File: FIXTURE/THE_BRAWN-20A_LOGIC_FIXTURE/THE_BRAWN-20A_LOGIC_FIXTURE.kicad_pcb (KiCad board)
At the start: 2 copper layers, 100 x 100 mm, 59 parts, among them J1 Pins_2.54_1x3, J2 Pins_2.54_1x3, J5 Pins_2.54_1x2, M1 Mount_M3, M10 Mount_M3, M11 Mount_M3, M12 Mount_M3, M13 Mount_M3, M14 Mount_M3, M2 Mount_M3, M3 Mount_M3, M4 Mount_M3, M5 Mount_M3, M6 Mount_M3, M7 Mount_M3, M8 Mount_M3, M9 Mount_M3

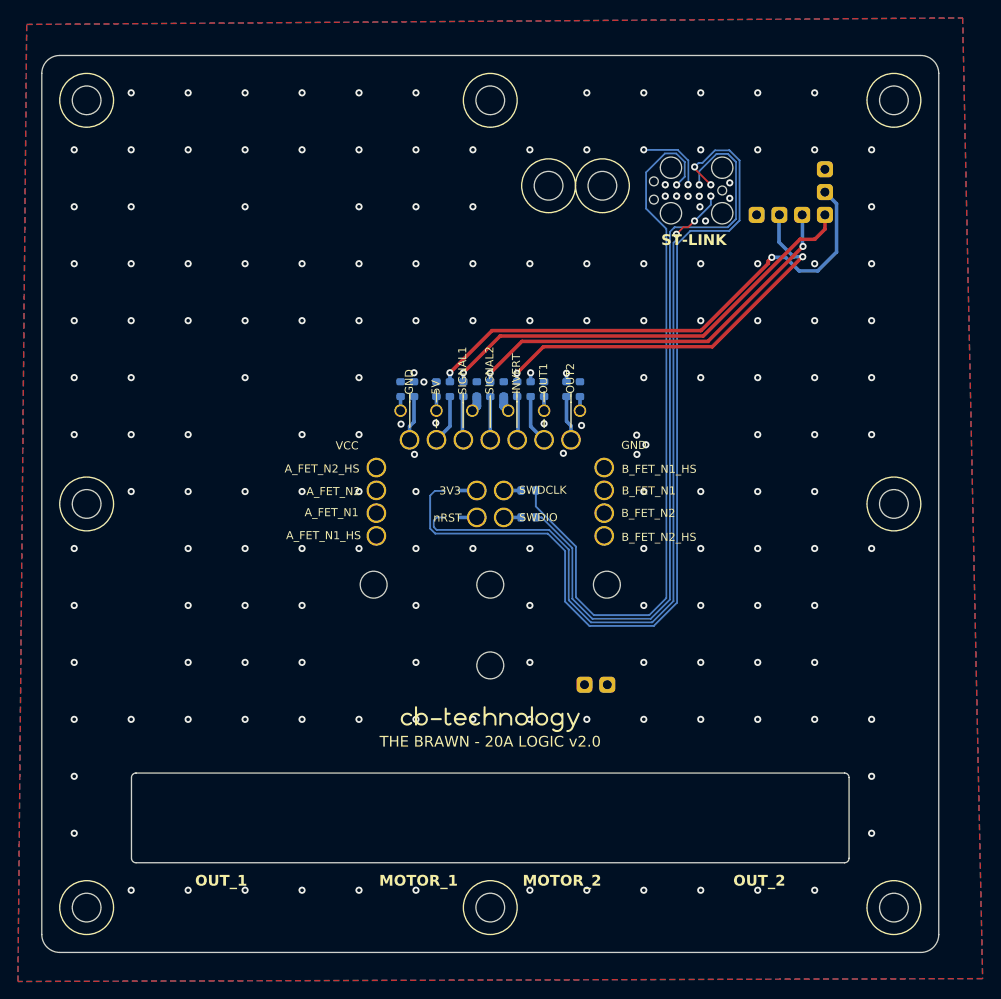
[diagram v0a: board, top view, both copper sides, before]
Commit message: Finish Tracking Logic Fixture PCB
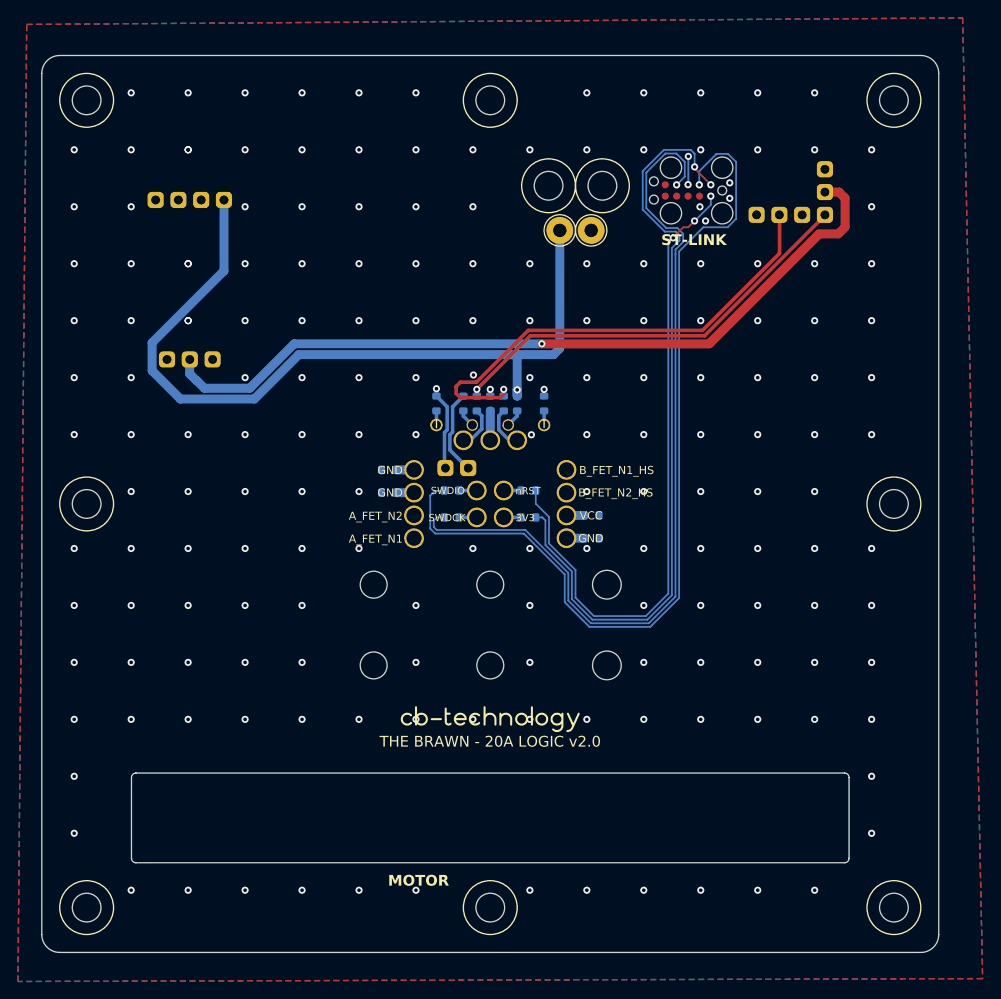
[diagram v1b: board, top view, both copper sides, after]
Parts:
- removed the R12 at (224.5, 127.2)
- removed the R13 at (228.5, 127.2)
- removed the TP14 at (210.0, 129.6)
- removed the TP15 at (214.0, 132.8)
- removed TP23, TP25, TP26, TP27: TestPoint, TestPoint:TestPoint_THTPad_D3.0mm_Drill1.5mm
- added J3: Pins_2.54_1x4, .J_Connector:Pins-2.54-1x4, B.Cu at (190.3, 106.1)
- added J4: Pins_2.54_1x3, .J_Connector:Pins-2.54-1x3, B.Cu at (189.0, 123.9)
- added M15: Mount_M3, .M_Mechanical:Mount_M3, F.Cu at (233.0, 149.0)
- added M16: Mount_M3, .M_Mechanical:Mount_M3, F.Cu at (233.0, 158.0)
- added R14: 0R, .R_Resistor:R_0603, B.Cu at (231.3, 141.3)
- added R15: 0R, .R_Resistor:R_0603, B.Cu at (231.3, 143.8)
- added TP16: TestPoint, TestPoint:TestPoint_THTPad_D3.0mm_Drill1.5mm, F.Cu at (227.8, 109.5)
- added TP17: TestPoint, TestPoint:TestPoint_THTPad_D3.0mm_Drill1.5mm, F.Cu at (231.2, 109.5)
- moved J5 28.7 mm to (215.0, 136.0)
- moved M14 27.5 mm to (207.0, 158.0)
- moved R6 20.2 mm to (215.7, 141.5), turned to 0 degrees
- moved R5 15.3 mm to (215.7, 138.5), turned to 0 degrees
- moved R2 12.7 mm to (208.7, 138.7), turned to 0 degrees
- moved TP13 12.0 mm to (223.0, 132.9)
- moved R1 9.09 mm to (208.7, 136.2), turned to 0 degrees
- moved R4 7.67 mm to (214.0, 128.8)
- moved R10 6.21 mm to (226.0, 128.8)
- moved R9 6.21 mm to (223.0, 128.8)
- moved R7 5.73 mm to (217.0, 128.8)
- moved R8 4.78 mm to (220.0, 128.8)
- moved TP19 4.21 mm to (228.5, 138.7)
- moved TP2 4.21 mm to (211.5, 138.7)
- moved TP1 4.21 mm to (211.5, 136.2)
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- renumbered R14 to R12, R15 to R13, TP2 to TP1, TP19 to TP10, TP22 to TP11, TP24 to TP12, TP6 to TP14, TP11 to TP15, TP9 to TP18, TP10 to TP19, TP3 to TP2, TP12 to TP20, TP20 to TP21, TP4 to TP3, TP21 to TP4, TP17 to TP5, TP16 to TP6, TP18 to TP7, TP5 to TP8, TP7 to TP9
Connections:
- J2 pad 1: /SIGNAL2 -> unconnected-(J2-Pad1)
- R12 pad 1: Net-(R14-Pad1) -> Net-(R12-Pad1)
- R12 pad 2: /VCC -> /nRST
- R13 pad 1: Net-(R15-Pad1) -> Net-(R13-Pad1)
- R13 pad 2: /GND -> /3V3
- R3 pad 2: /GND -> /SIGNAL1
- R6 pad 1: /SWCLK -> /SWDCLK
- R8 pad 2: /SIGNAL1 -> /GND
- TP1 pad 1: Net-(R2-Pad2) -> Net-(R1-Pad2)
- TP10 pad 1: /B_FET_N1 -> Net-(R8-Pad1)
- TP11 pad 1: Net-(R4-Pad1) -> Net-(R9-Pad1)
- TP12 pad 1: Net-(R5-Pad1) -> Net-(R10-Pad1)
- TP14 pad 1: Net-(R4-Pad1) -> Net-(R12-Pad1)
- TP15 pad 1: Net-(R9-Pad1) -> Net-(R13-Pad1)
- TP18 pad 1: Net-(R6-Pad2) -> /B_FET_N1_HS
- TP19 pad 1: Net-(R8-Pad1) -> /B_FET_N2_HS
- TP2 pad 1: /A_FET_N2 -> Net-(R2-Pad2)
- TP20 pad 1: Net-(R10-Pad1) -> Net-(R14-Pad1)
- TP21 pad 1: Net-(R14-Pad1) -> Net-(R15-Pad1)
- TP3 pad 1: /A_FET_N1 -> /A_FET_N2
- TP4 pad 1: Net-(R15-Pad1) -> /A_FET_N1
- TP5 pad 1: /GND -> Net-(R3-Pad1)
- TP6 pad 1: /BATT+ -> Net-(R4-Pad1)
- TP7 pad 1: /B_FET_N1 -> Net-(R7-Pad1)
- TP8 pad 1: Net-(R3-Pad1) -> Net-(R5-Pad2)
- TP9 pad 1: Net-(R7-Pad1) -> Net-(R6-Pad2)
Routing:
- net /BATT+: track 0.00 -> 91.9 mm, vias 0 -> 1
- net /SIGNAL2: track 45.3 -> 0.00 mm, vias 2 -> 0
- net /5V0: track 58.3 -> 88.5 mm, vias 2 -> 1
- net /3V3: track 106.6 -> 85.6 mm, vias 3 -> 2
- net /SWDIO: track 85.9 -> 100.6 mm
- net /nRST: track 85.7 -> 72.6 mm, vias 4 -> 3
- net /SWDCLK: track 82.3 -> 95.1 mm
- net /INVERT: track 44.6 -> 54.5 mm, vias 2 -> 1
- net /MOTOR_1-: track 0.00 -> 9.51 mm
- net /MOTOR_1+: track 0.00 -> 9.51 mm, vias 0 -> 1
- net Net-(R7-Pad1): track 6.96 -> 1.99 mm
- net Net-(R12-Pad1): track 5.45 -> 1.93 mm
- net /GND: track 8.17 -> 4.83 mm, vias 170 -> 182
- net Net-(R10-Pad1): track 4.86 -> 1.57 mm
- net (no net): track 3.19 -> 0.00 mm
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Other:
- board text added: "5V"
- board text added: "B+"
- board text added: "B-"
- board text added: "G"
- board text added: "MOTOR"
- board text added: "S"
- board text added: "SERVO/BEC"
- board text added: "SWDCK"
- board text removed: "-5V"
- board text removed: "-GND"
- board text removed: "-INVERT"
- board text removed: "-OUT1"
- board text removed: "-OUT2"
- board text removed: "-SIGNAL1"
- board text removed: "-SIGNAL2"
- board text removed: "A_FET_N1_HS"
- board text removed: "A_FET_N2_HS"
- board text removed: "B_FET_N1"
- board text removed: "B_FET_N2"
- board text removed: "MOTOR_1"
- board text removed: "MOTOR_2"
- board text removed: "OUT_1"
- board text removed: "OUT_2"
- board text removed: "SERVO2"
- board text removed: "SWDCLK"
